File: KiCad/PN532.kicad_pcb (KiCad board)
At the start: 2 copper layers, 42 x 42 mm, 48 parts, among them J1 Bell, J2 Header, J3 SPOX, J4 MiniGrid, SW1 TAMPER, U1 PN532, U2 QR, Y1 27.12MHz

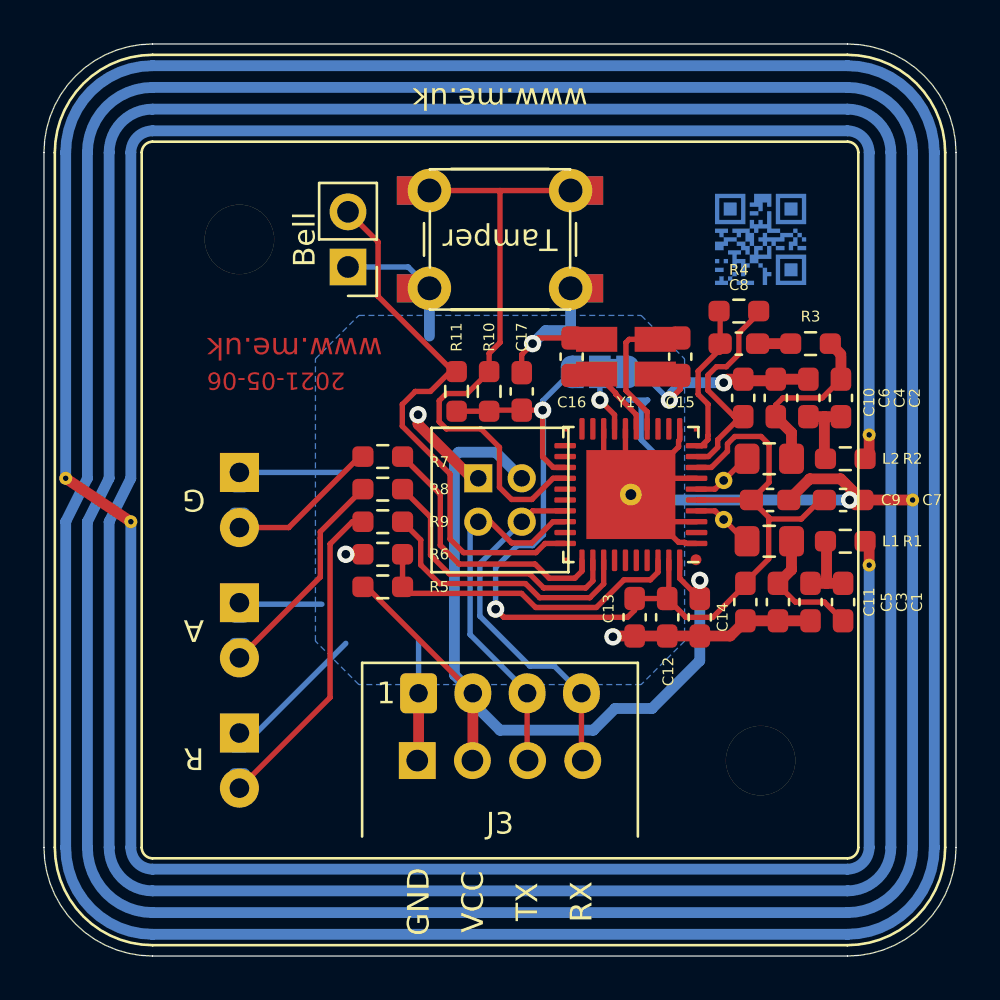
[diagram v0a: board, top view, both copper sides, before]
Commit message: Back to later antenna as it is better, waiting on RF work to fine tune
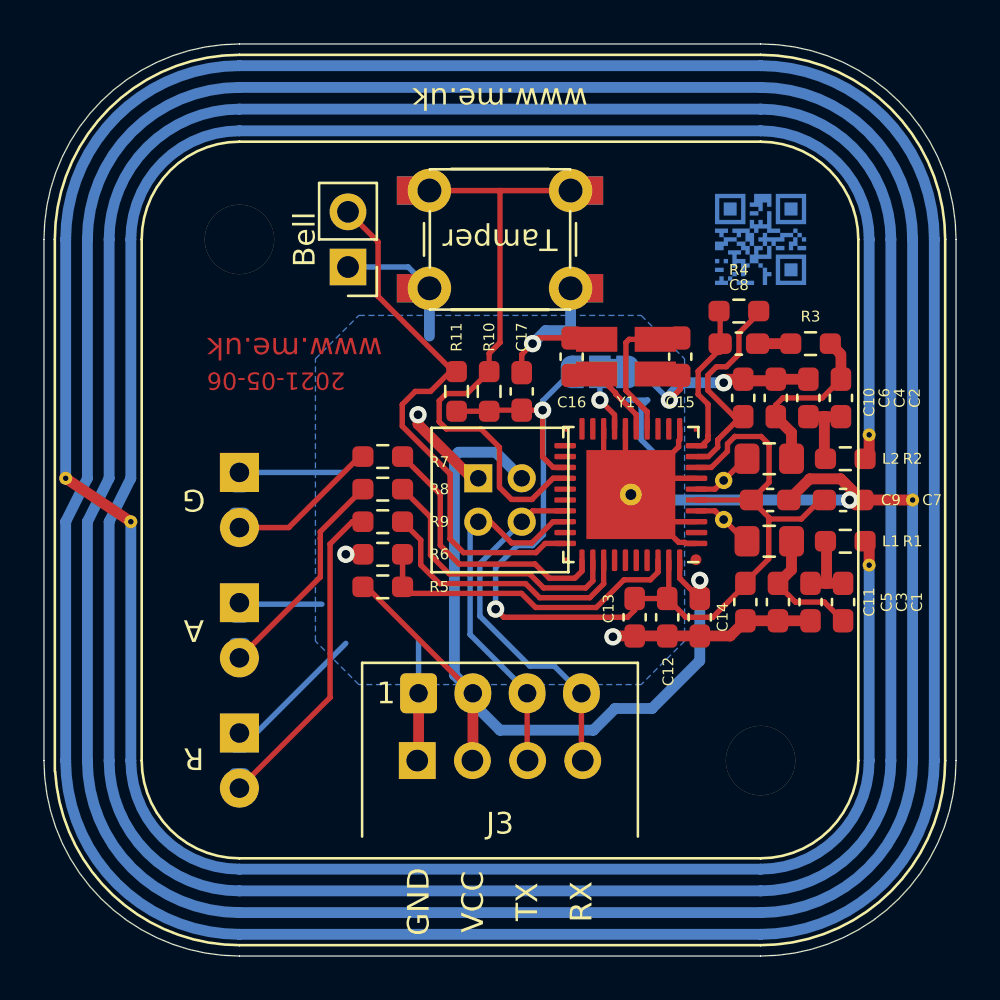
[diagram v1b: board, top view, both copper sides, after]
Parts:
- A1: footprint RevK:PN532-Antenna -> RevK:PN532-Antenna3
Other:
- outline, holes or cut-outs redrawn

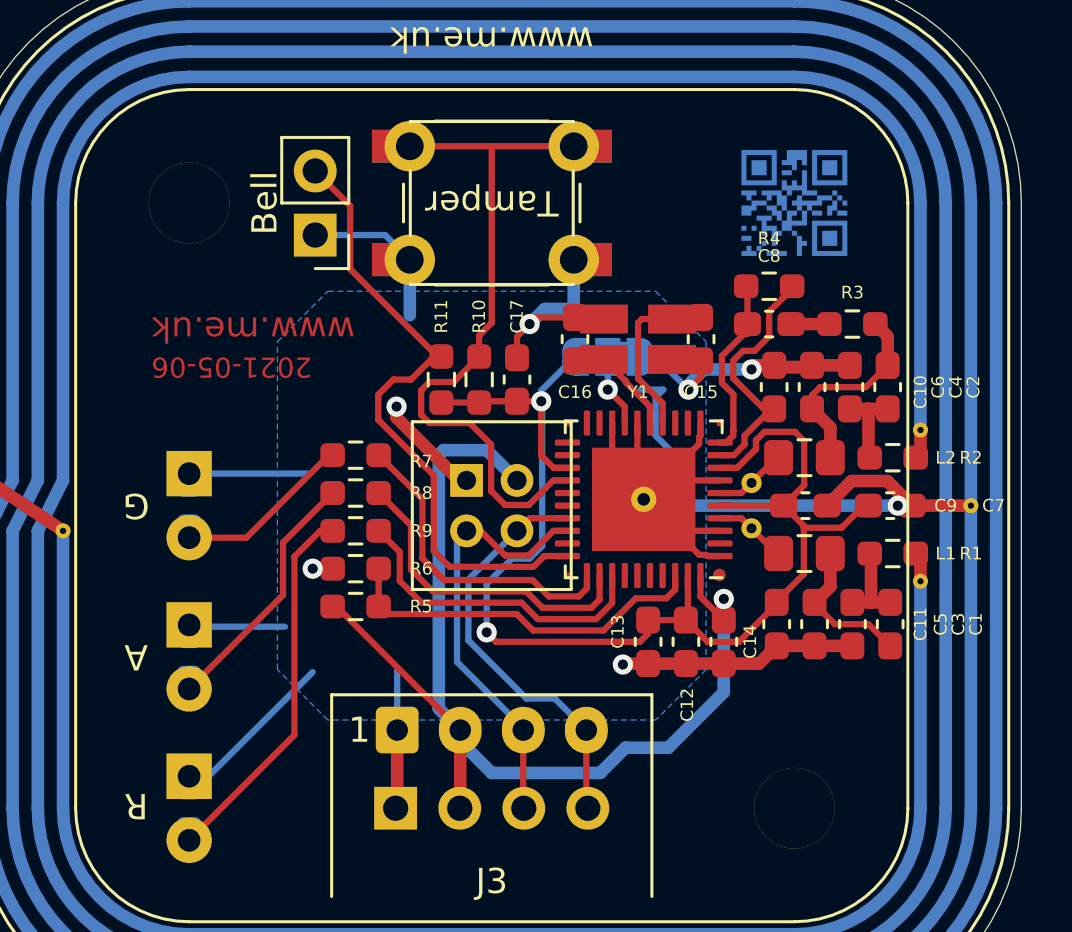
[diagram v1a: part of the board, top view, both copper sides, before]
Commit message: Change to 1206 pads for inductor
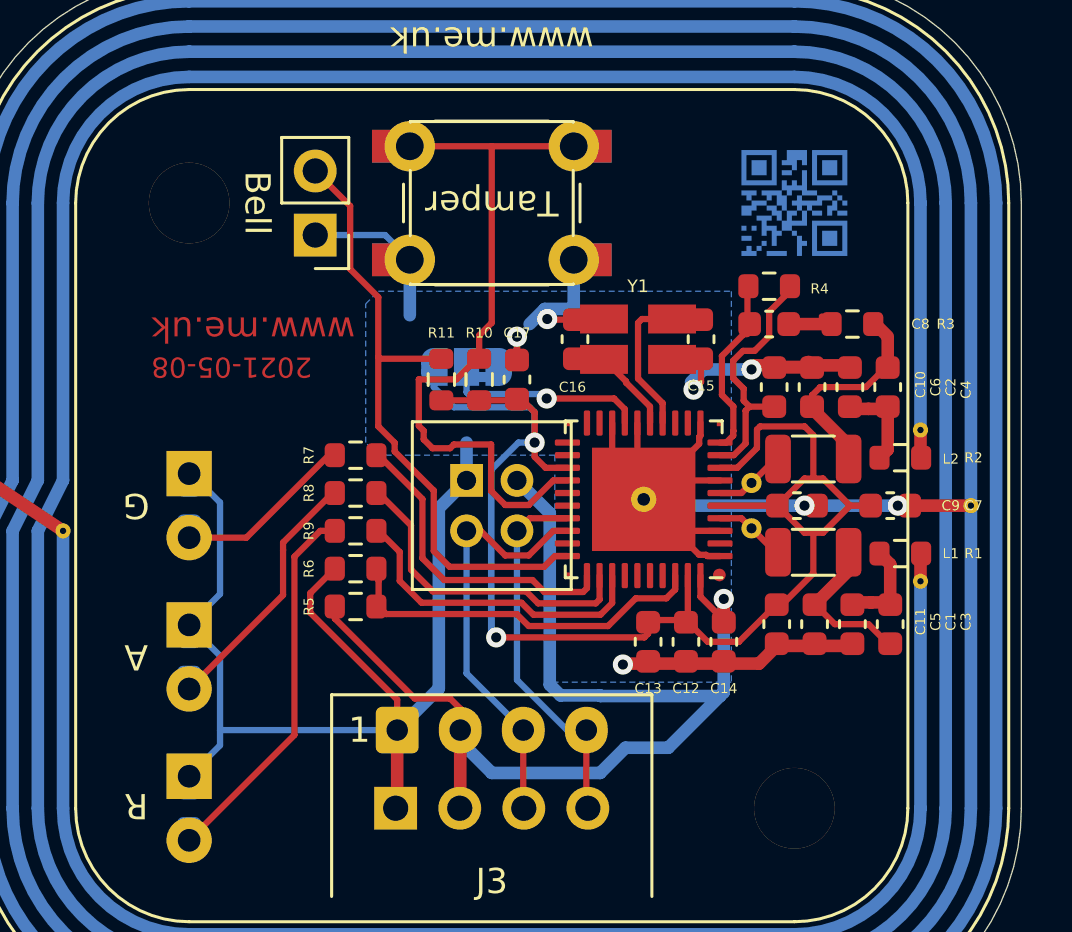
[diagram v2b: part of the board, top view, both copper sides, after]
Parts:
- C1, C10, C11, C12, C13, C14, C15, C16, C17, C2, C3, C4, C5, C6, C7, C8, C9: footprint Capacitor_SMD:C_0603_1608Metric_Pad1.08x0.95mm_HandSolder -> Capacitor_SMD:C_0603_1608Metric
- L1, L2: footprint Inductor_SMD:L_0805_2012Metric_Pad1.15x1.40mm_HandSolder -> RevK:L_1206_3216Metric
- R1, R10, R11, R2, R3, R4, R5, R6, R7, R8, R9: footprint Resistor_SMD:R_0603_1608Metric_Pad0.98x0.95mm_HandSolder -> Resistor_SMD:R_0603_1608Metric
- moved JP1 5.61 mm to (149.0, 89.5)
- moved L1 0.35 mm to (162.8, 96.8)
- moved L2 0.35 mm to (162.8, 93.2)
- moved C9 0.34 mm to (162.1, 95.0)
- moved R1 0.30 mm to (166.2, 96.9)
- moved R2 0.30 mm to (166.2, 93.1)
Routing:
- net +3V3: track 53.0 -> 66.1 mm
- net GND: track 111.9 -> 122.5 mm
- net Net-(JP1-Pad2): track 2.90 -> 8.10 mm
- net Net-(J2-Pad4): track 16.6 -> 14.8 mm
- net +5V: track 45.2 -> 46.7 mm
- net Net-(R10-Pad2): track 27.7 -> 28.8 mm
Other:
- board text added: "2021-05-08"
- board text removed: "2021-05-06"

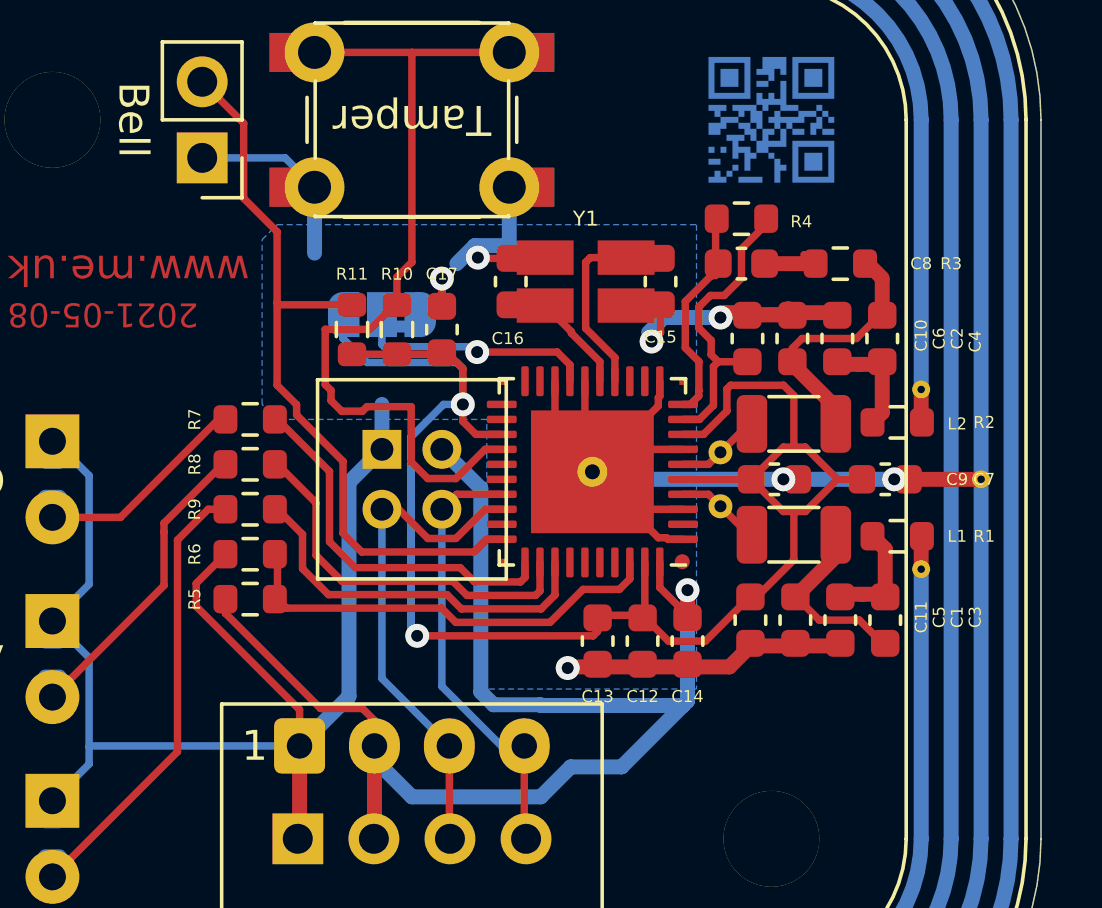
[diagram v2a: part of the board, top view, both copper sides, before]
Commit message: Tidy a bit with smaller ground plane
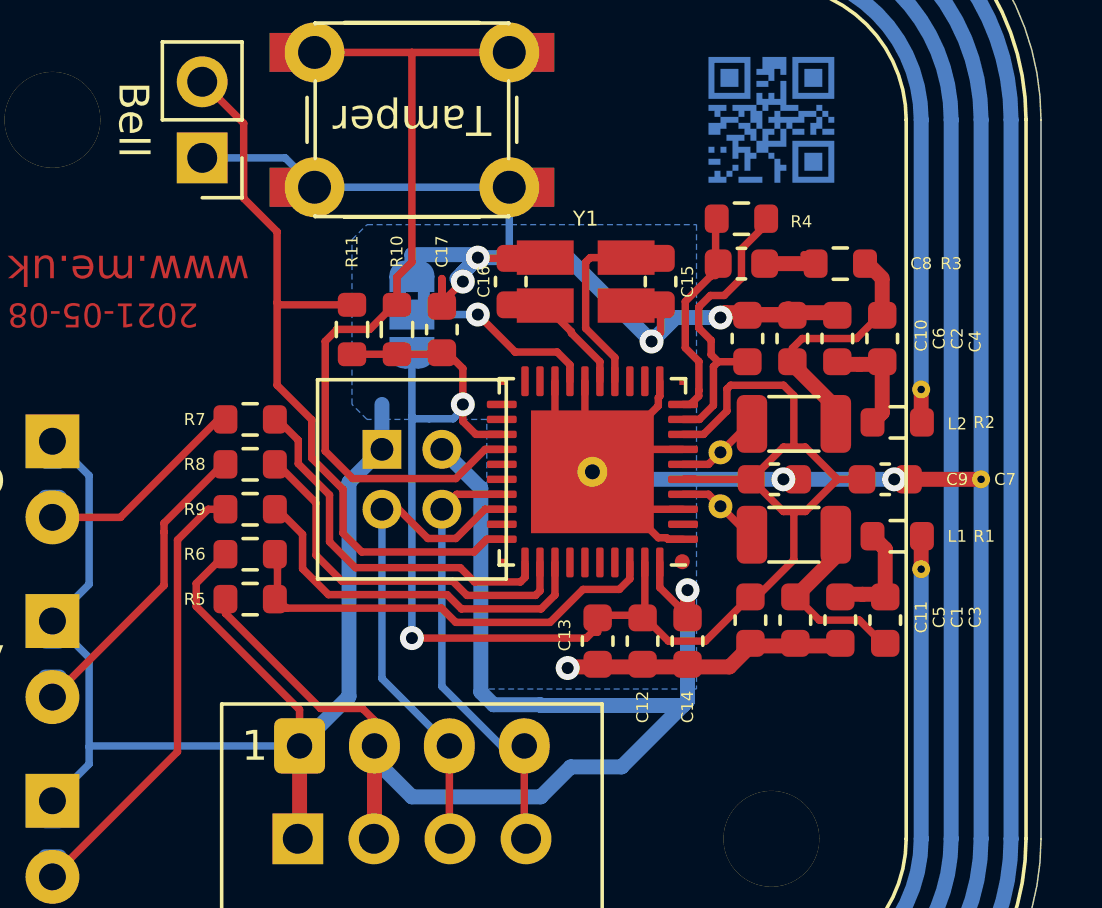
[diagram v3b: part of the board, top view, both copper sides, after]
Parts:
- moved JP1 1.00 mm to (150.0, 89.5), turned to 270 degrees
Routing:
- net GND: track 122.5 -> 136.6 mm
- net +3V3: track 66.1 -> 55.0 mm
- net Net-(JP1-Pad2): track 8.10 -> 6.52 mm

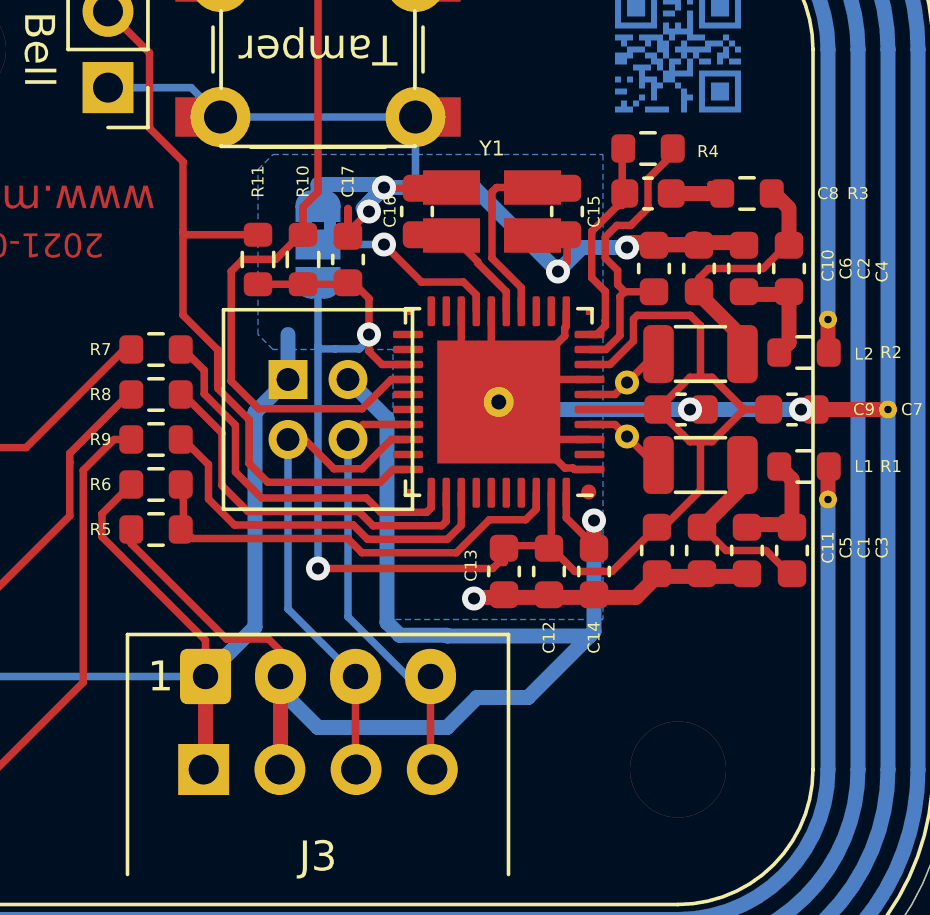
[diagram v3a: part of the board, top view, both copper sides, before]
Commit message: More space around inductor.
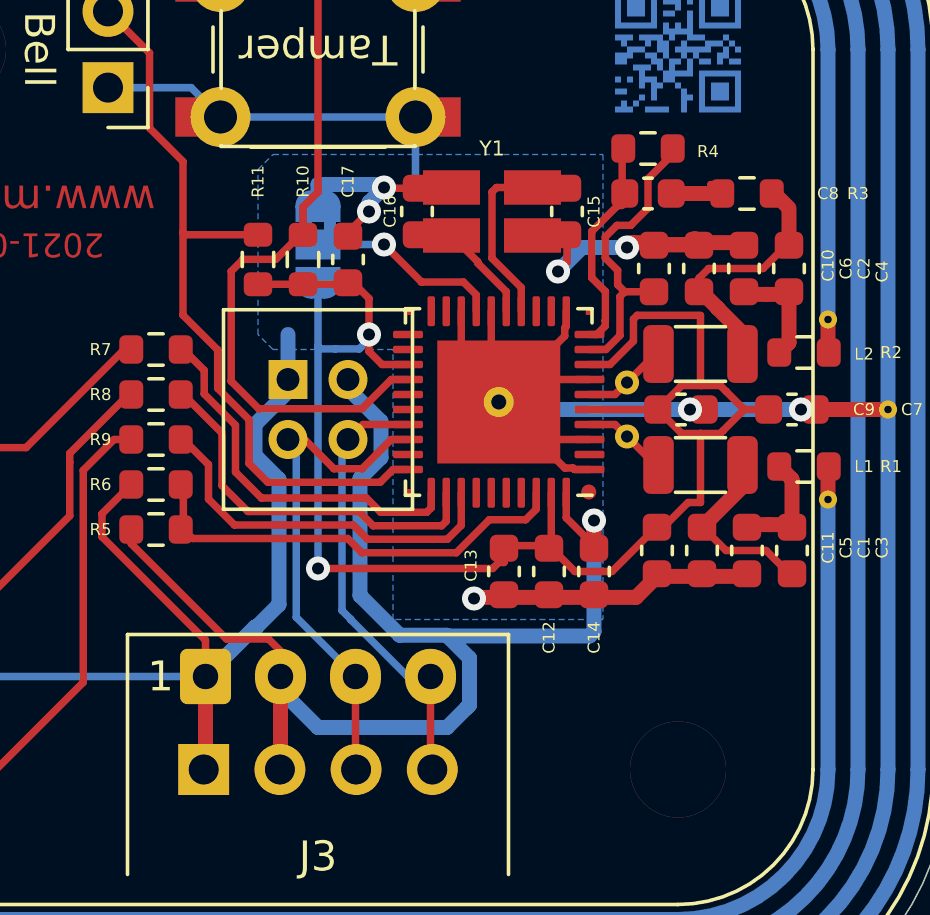
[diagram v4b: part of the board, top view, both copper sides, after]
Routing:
- net GND: track 136.6 -> 127.6 mm
- net +5V: track 46.7 -> 44.9 mm
- net +3V3: track 55.0 -> 55.5 mm

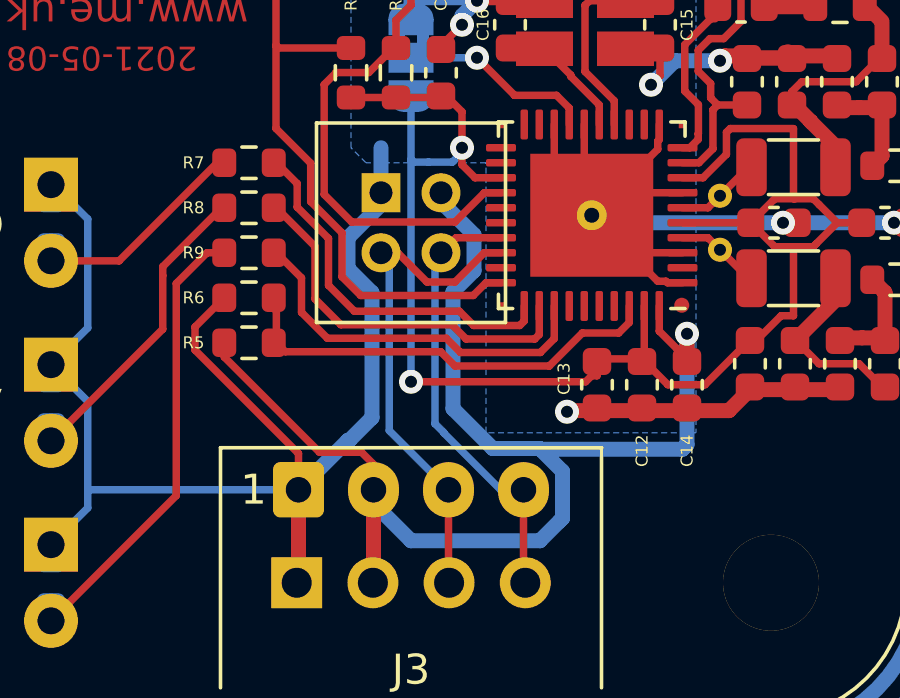
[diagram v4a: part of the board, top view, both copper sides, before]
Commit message: Some advice re RF leading to tweaks to ground plane.
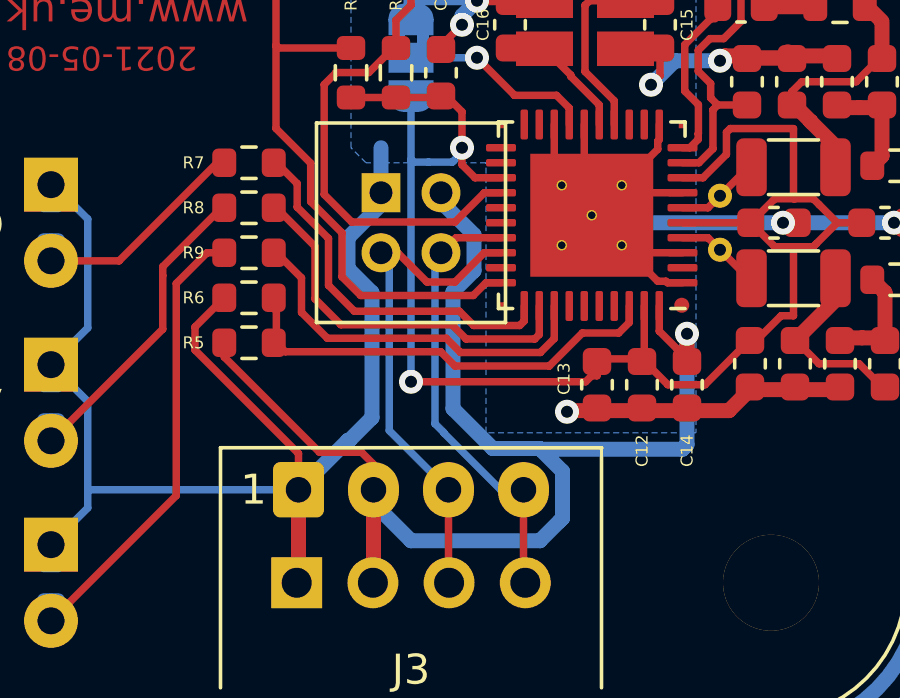
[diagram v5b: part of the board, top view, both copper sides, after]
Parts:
- added ?: , , F.Cu at (156.2, 85.2)
- added ?: , , F.Cu at (157.0, 86.5)
